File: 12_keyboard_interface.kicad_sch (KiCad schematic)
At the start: 40 parts, among them J310 Mainboard keyboard FFC to MX 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, U310 TPS2553D keyboard RGB 5V swit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, U311 SN74AHCT1G126 keyboard RGB 3V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

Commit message: add rgb to the keyboard and get it ready to route
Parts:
- R387: value 0R DNP keyboard 3V3 option -> 0R keyboard RGB bus-buffer supply; MPN (none) -> RC0603JR-070RL; Manufacturer (none) -> Yageo; now fitted; now in the parts list
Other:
- note added: "J310 pin 3 / J320 pin 28 is an unused one-wire data option. The RGB keyboard uses I2C on J320 pins 3/4."
- note added: "R386 stays DNP. Fit R387 for the RGB keyboard bus buffer. U310 limits the switched 5 V rail and defaults off."
- note added: "RGB keyboard U320 uses a 33.2k current-setting resistor. Budget 0.25A on the switched 5V feed and verify full-white current on hardware."
- note removed: "J310 pin 3 / rev-A J320 pin 28 repurposes unused COL15 for RGB data. Rows 5..7 and COL14 remain spare."
- note removed: "R386/R387 stay DNP. U310 limits the future RGB rail below 0.5A/contact and defaults off; rev A has no RGB load."
- note removed: "Rev B must add local LED bulk capacitance and firmware must enforce a 325mA LED budget; unrestricted full-white is unsupported."
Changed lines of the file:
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@@
   (unit 1)
   (exclude_from_sim no)
-  (in_bom no)
+  (in_bom yes)
   (on_board yes)
-  (dnp yes)
+  (dnp no)
   (property "Reference" "R387" (at 449.58 102.87 0) (effects (font (size 1.27 1.27))))
-  (property "Value" "0R DNP keyboard 3V3 option" (at 449.58 107.95 0) (effects (font (size 1.27 1.27))))
+  (property "Value" "0R keyboard RGB bus-buffer supply" (at 449.58 107.95 0) (effects (font (size 1.27 1.27))))
   (property "Footprint" "Resistor_SMD:R_0603_1608Metric" (at 449.58 105.41 0) (effects (font (size 1.27 1.27)) (hide yes)))
   (property "Datasheet" "" (at 449.58 105.41 0) (effects (font (size 1.27 1.27)) (hide yes)))
+  (property "Manufacturer" "Yageo" (at 449.58 105.41 0) (effects (font (size 1.27 1.27)) (hide yes)))
+  (property "MPN" "RC0603JR-070RL" (at 449.58 105.41 0) (effects (font (size 1.27 1.27)) (hide yes)))
   (pin "1")
   (pin "2")
@@
 (text "J310 is deliberately pin-reversed relative to J320 for two top-side FH12 bottom-contact connectors and a Type-A same-side FFC." (at 20.32 237.49 0) (effects (font (size 1.27 1.27))))
 (text "Specified cable: Molex 0150200315, 30 circuits, 0.5 mm pitch, 30 mm, Type A / same-side contacts." (at 20.32 245.11 0) (effects (font (size 1.27 1.27))))
-(text "R386/R387 stay DNP. U310 limits the future RGB rail below 0.5A/contact and defaults off; rev A has no RGB load." (at 20.32 252.73 0) (effects (font (size 1.27 1.27))))
-(text "J310 pin 3 / rev-A J320 pin 28 repurposes unused COL15 for RGB data. Rows 5..7 and COL14 remain spare." (at 20.32 260.35 0) (effects (font (size 1.27 1.27))))
-(text "Rev B must add local LED bulk capacitance and firmware must enforce a 325mA LED budget; unrestricted full-white is unsupported." (at 20.32 267.97 0) (effects (font (size 1.27 1.27))))
+(text "R386 stays DNP. Fit R387 for the RGB keyboard bus buffer. U310 limits the switched 5 V rail and defaults off." (at 20.32 252.73 0) (effects (font (size 1.27 1.27))))
+(text "J310 pin 3 / J320 pin 28 is an unused one-wire data option. The RGB keyboard uses I2C on J320 pins 3/4." (at 20.32 260.35 0) (effects (font (size 1.27 1.27))))
+(text "RGB keyboard U320 uses a 33.2k current-setting resistor. Budget 0.25A on the switched 5V feed and verify full-white current on hardware." (at 20.32 267.97 0) (effects (font (size 1.27 1.27))))
 (sheet_instances
   (path "/cb7351cd-fcb6-573d-ba16-39cf42fd14a4"

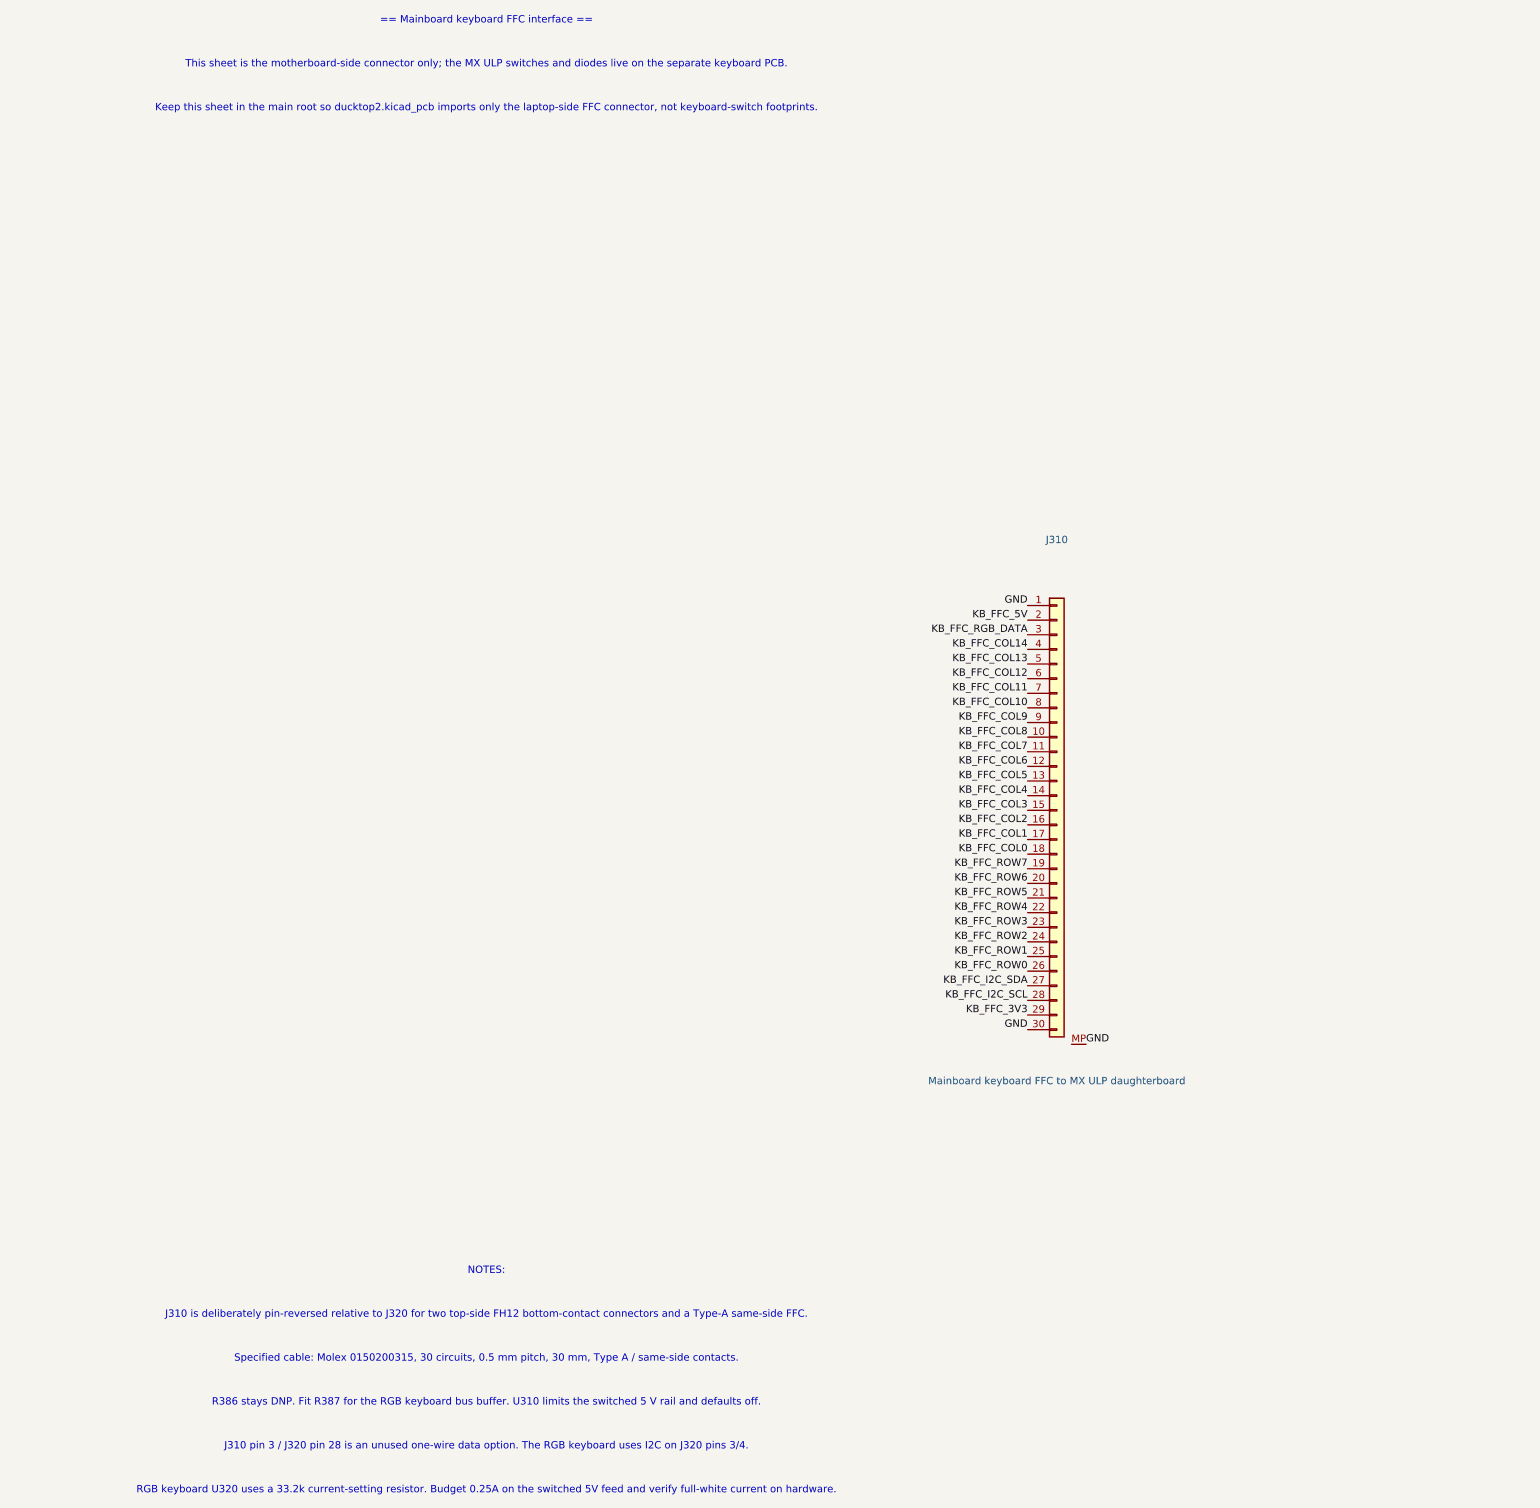
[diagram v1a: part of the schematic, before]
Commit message: finish the new bms and move the connectors up top
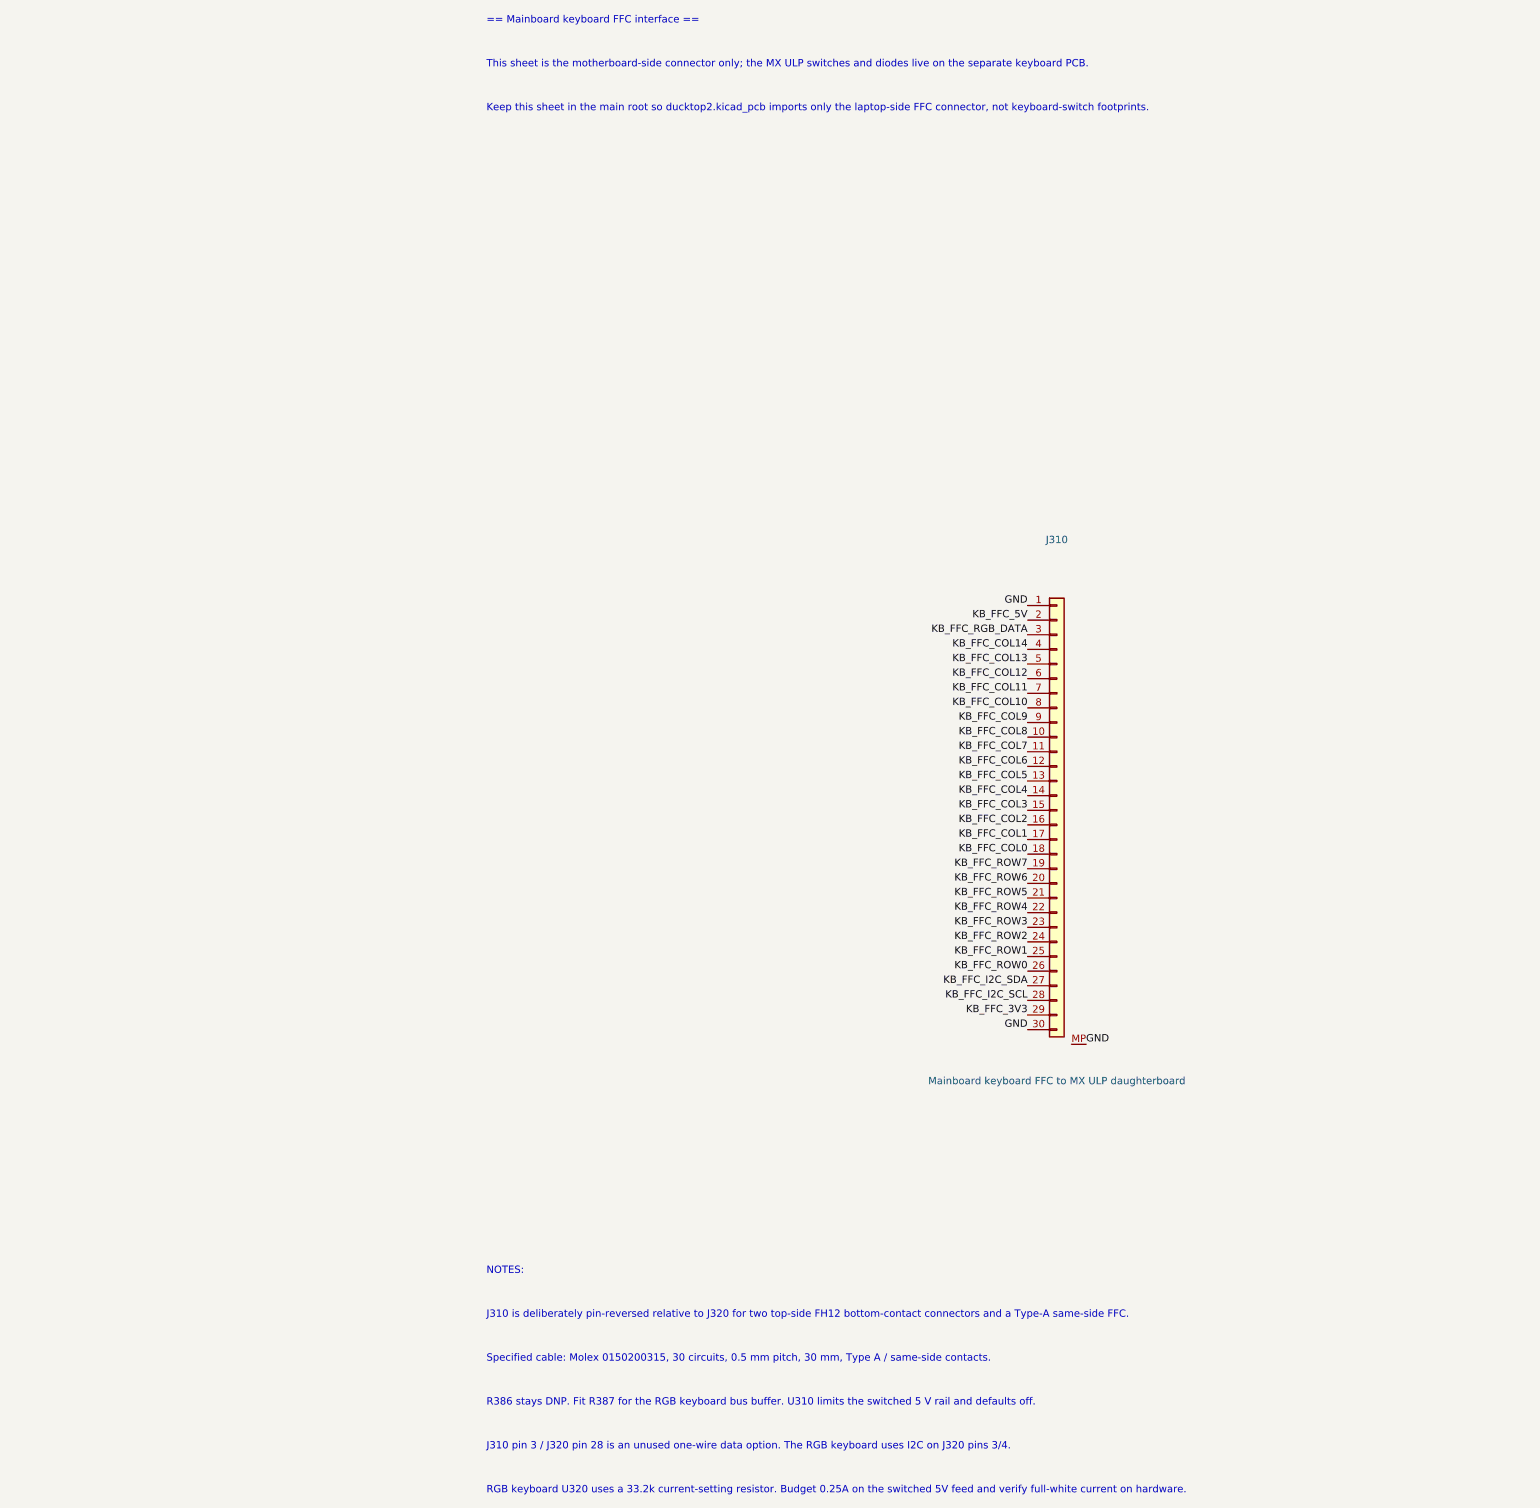
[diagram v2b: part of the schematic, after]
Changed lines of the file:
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@@
   (generator_version "10.0")
   (paper "A2")
-(text "== Mainboard keyboard FFC interface ==" (at 20.32 12.7 0) (effects (font (size 1.27 1.27))))
-(text "This sheet is the motherboard-side connector only; the MX ULP switches and diodes live on the separate keyboard PCB." (at 20.32 20.32 0) (effects (font (size 1.27 1.27))))
-(text "Keep this sheet in the main root so ducktop2.kicad_pcb imports only the laptop-side FFC connector, not keyboard-switch footprints." (at 20.32 27.94 0) (effects (font (size 1.27 1.27))))
+(text "== Mainboard keyboard FFC interface ==" (at 20.32 12.7 0) (effects (font (size 1.27 1.27)) (justify left)))
+(text "This sheet is the motherboard-side connector only; the MX ULP switches and diodes live on the separate keyboard PCB." (at 20.32 20.32 0) (effects (font (size 1.27 1.27)) (justify left)))
+(text "Keep this sheet in the main root so ducktop2.kicad_pcb imports only the laptop-side FFC connector, not keyboard-switch footprints." (at 20.32 27.94 0) (effects (font (size 1.27 1.27)) (justify left)))
 (symbol
   (lib_id "Conn_01x30_FFC_MP:Conn_01x30_FFC_MP")
@@
   (effects (font (size 1.27 1.27)) (justify left bottom))
 )
-(text "NOTES:" (at 20.32 229.87 0) (effects (font (size 1.27 1.27))))
-(text "J310 is deliberately pin-reversed relative to J320 for two top-side FH12 bottom-contact connectors and a Type-A same-side FFC." (at 20.32 237.49 0) (effects (font (size 1.27 1.27))))
-(text "Specified cable: Molex 0150200315, 30 circuits, 0.5 mm pitch, 30 mm, Type A / same-side contacts." (at 20.32 245.11 0) (effects (font (size 1.27 1.27))))
-(text "R386 stays DNP. Fit R387 for the RGB keyboard bus buffer. U310 limits the switched 5 V rail and defaults off." (at 20.32 252.73 0) (effects (font (size 1.27 1.27))))
-(text "J310 pin 3 / J320 pin 28 is an unused one-wire data option. The RGB keyboard uses I2C on J320 pins 3/4." (at 20.32 260.35 0) (effects (font (size 1.27 1.27))))
-(text "RGB keyboard U320 uses a 33.2k current-setting resistor. Budget 0.25A on the switched 5V feed and verify full-white current on hardware." (at 20.32 267.97 0) (effects (font (size 1.27 1.27))))
+(text "NOTES:" (at 20.32 229.87 0) (effects (font (size 1.27 1.27)) (justify left)))
+(text "J310 is deliberately pin-reversed relative to J320 for two top-side FH12 bottom-contact connectors and a Type-A same-side FFC." (at 20.32 237.49 0) (effects (font (size 1.27 1.27)) (justify left)))
+(text "Specified cable: Molex 0150200315, 30 circuits, 0.5 mm pitch, 30 mm, Type A / same-side contacts." (at 20.32 245.11 0) (effects (font (size 1.27 1.27)) (justify left)))
+(text "R386 stays DNP. Fit R387 for the RGB keyboard bus buffer. U310 limits the switched 5 V rail and defaults off." (at 20.32 252.73 0) (effects (font (size 1.27 1.27)) (justify left)))
+(text "J310 pin 3 / J320 pin 28 is an unused one-wire data option. The RGB keyboard uses I2C on J320 pins 3/4." (at 20.32 260.35 0) (effects (font (size 1.27 1.27)) (justify left)))
+(text "RGB keyboard U320 uses a 33.2k current-setting resistor. Budget 0.25A on the switched 5V feed and verify full-white current on hardware." (at 20.32 267.97 0) (effects (font (size 1.27 1.27)) (justify left)))
 (sheet_instances
   (path "/cb7351cd-fcb6-573d-ba16-39cf42fd14a4"
